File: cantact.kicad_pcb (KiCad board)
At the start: 2 copper layers, 36 x 16.4 mm, 38 parts, among them J1 USB_C_Receptacle_USB2.0, J2 Conn_01x04, J3 Conn_01x06, SW1 SW_SPST, SW2 SW_DPDT_x2, U1 NJM2871, U2 STM32F042C6Ux, U3 MCP2562-E-MF, Y1 Resonator

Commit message: 電源LEDの配置いじった
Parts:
- C1, R4: moved to B.Cu
- SW1: value SW_SPST -> SKRPACE010; footprint Button_Switch_SMD:SW_SPST_B3U-1000P -> Button_Switch_SMD_my:ALPS_SKRPAxE010
- moved D1 14.3 mm to (159.8, 111.4), turned to 180 degrees
- moved R3 12.7 mm to (163.2, 111.2)
- moved R7 8.86 mm to (155.6, 114.6)
- moved C2 4.85 mm to (164.6, 123.5), turned to 270 degrees
- moved C3 4.61 mm to (159.9, 123.5), turned to 270 degrees
- moved SW1 4.30 mm to (141.2, 123.2), turned to 180 degrees
- moved J2 2.01 mm to (147.5, 118.8)
- moved SW2 2.01 mm to (144.0, 116.4)
- moved C1 1.93 mm to (162.1, 123.8), turned to 90 degrees
- moved R9 1.41 mm to (144.3, 111.2)
- moved C16 1.07 mm to (154.0, 112.2), turned to 180 degrees
- moved C15 1.00 mm to (150.4, 110.7), turned to 0 degrees
- moved R8 0.85 mm to (149.8, 112.8), turned to 270 degrees
- moved L1 0.71 mm to (160.4, 121.0), turned to 270 degrees
- moved U3 0.55 mm to (152.4, 111.2)
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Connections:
- net Net-(J2-Pad2) renamed /CAN_+
- net Net-(J2-Pad3) renamed /CAN_-
- SW1 pad 2: Net-(R7-Pad1) -> (no net)
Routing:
- net GND: track 86.7 -> 151.4 mm, vias 30 -> 61
- net +5V: track 30.3 -> 35.8 mm
- net Net-(R7-Pad1): track 16.3 -> 19.7 mm
- net Net-(D4-Pad1): track 0.00 -> 2.87 mm
- net /CAN_-: track 8.04 -> 10.9 mm
- net Net-(R4-Pad2): track 5.88 -> 7.95 mm
- net +3V3: track 62.6 -> 60.8 mm, vias 7 -> 6
- net SWCLK: track 4.58 -> 2.92 mm
- net Net-(R5-Pad2): track 1.22 -> 2.49 mm
- net NRST: track 16.9 -> 18.0 mm
- net Net-(D1-Pad1): track 1.49 -> 2.21 mm
- net /CAN_+: track 8.95 -> 9.63 mm
- net SWDIO: track 9.48 -> 9.41 mm, vias 3 -> 1
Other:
- board size 36 x 16.4 mm -> 33 x 16.4 mm
- board text added: "+5V"
- board text added: "BOOT"
- board text added: "CAN"
- board text added: "Terminate"
- board text removed: "5V"
- board text removed: "BOOT0"
- board text removed: "SWCLK"
- board text removed: "Vtgt"

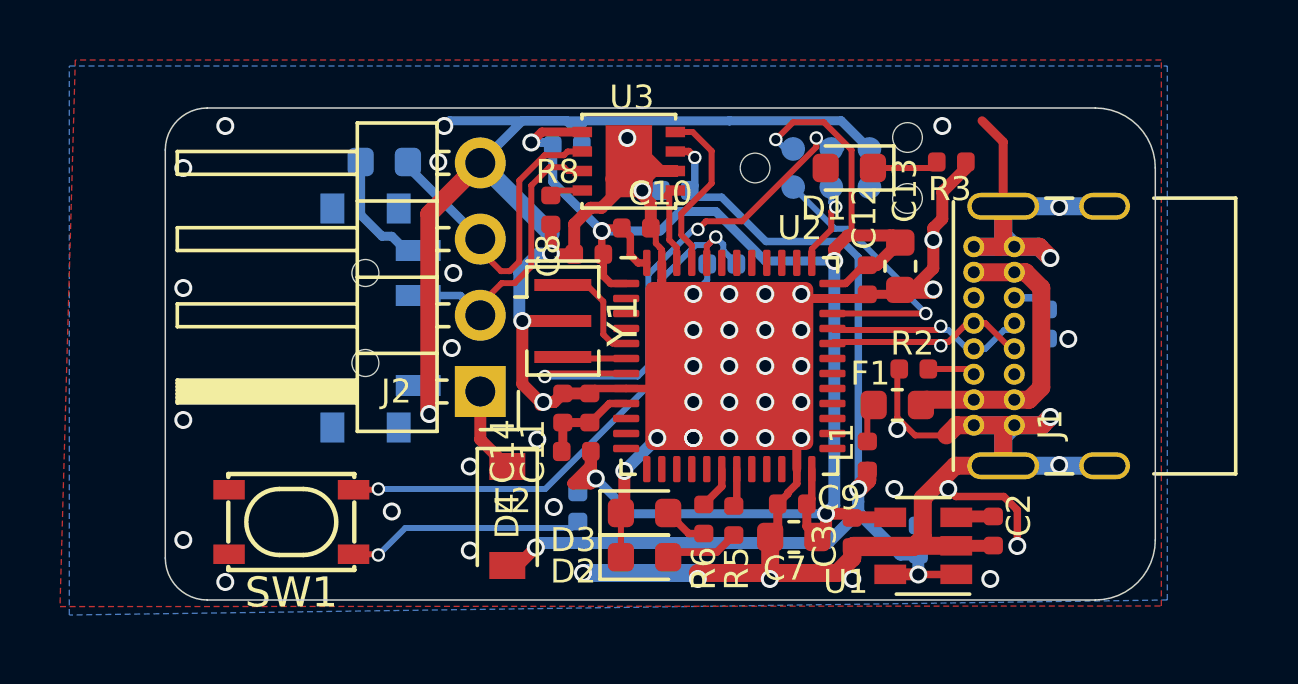
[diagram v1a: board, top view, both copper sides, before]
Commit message: 不要なシルクは全部非表示にした
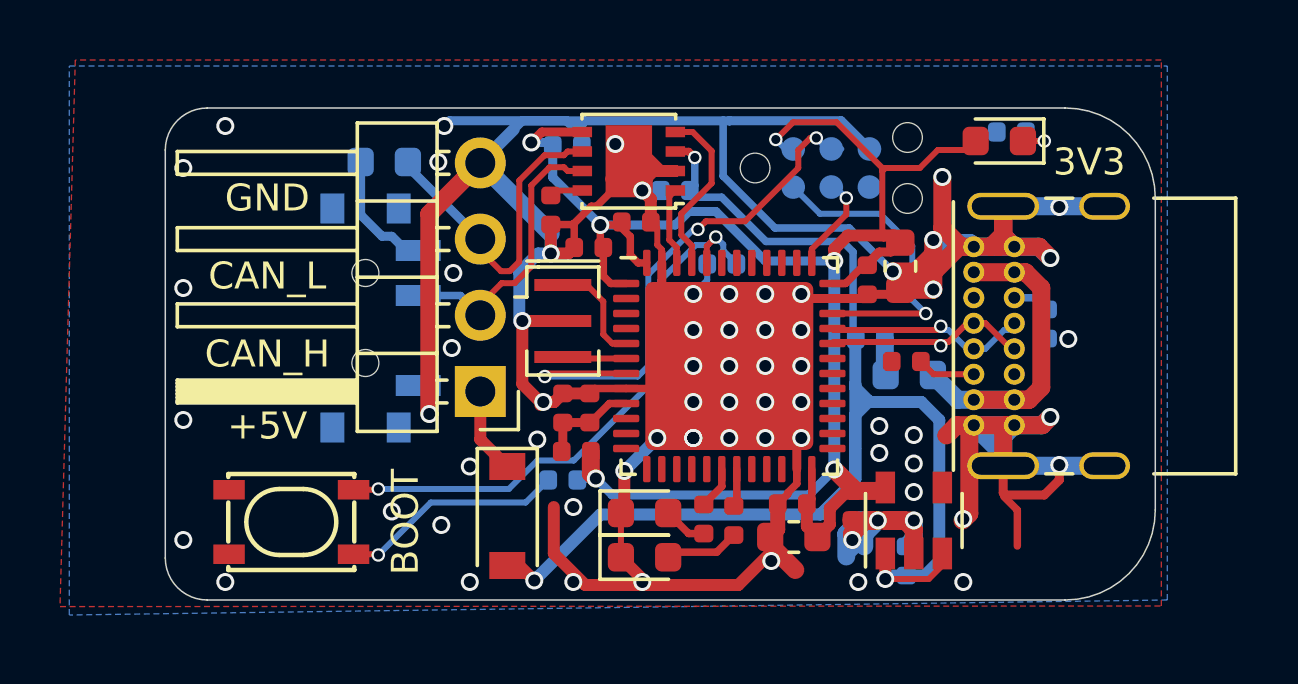
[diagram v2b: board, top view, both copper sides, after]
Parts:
- removed C2: 0.01u, Capacitor_SMD:C_0402_1005Metric
- C1: value 0.1u -> 1u
- F1, L1, R3: moved to B.Cu
- R9: value R -> 120
- U1: value NJM2871 -> MIC5365-3.3YD5
- moved D1 5.08 mm to (164.8, 110.5)
- moved L1 3.90 mm to (160.5, 117.1), turned to 180 degrees
- moved R3 2.24 mm to (165.2, 110.2), turned to 180 degrees
- moved F1 1.08 mm to (161.8, 118.3)
- moved R4 1.03 mm to (150.2, 121.8), turned to 180 degrees
- moved U1 0.90 mm to (161.9, 123.2), turned to 90 degrees
- moved C3 0.90 mm to (159.9, 122.7)
- moved C1 0.81 mm to (161.7, 124.5)
- moved R2 0.35 mm to (161.7, 117.8)
- moved C8 0.23 mm to (151.1, 114.0)
- moved C10 0.20 mm to (152.7, 113.2)
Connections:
- U1 pad 3: Net-(C2-Pad1) -> +5V
- U1 pad 4: +3V3 -> (no net)
- U1 pad 5: +5V -> +3V3
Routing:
- net GND: track 151.4 -> 170.1 mm, vias 61 -> 68
- net +5V: track 35.8 -> 45.3 mm, vias 4 -> 3
- net +3V3: track 60.8 -> 63.0 mm
- net Net-(F1-Pad2): track 10.0 -> 11.8 mm
- net Net-(C2-Pad1): track 1.29 -> 0.00 mm
- net SWDIO: track 9.41 -> 10.3 mm
- net Net-(D1-Pad1): track 2.21 -> 1.45 mm, vias 0 -> 1
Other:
- outline, holes or cut-outs redrawn
- board text added: "3V3"
- board text added: "CAN_Termination"
- board text removed: "CAN"
- board text removed: "Terminate"
